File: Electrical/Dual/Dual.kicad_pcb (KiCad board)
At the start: 2 copper layers, 140 x 70 mm, 193 parts, among them J101 01x04, J102 02x04, J103 01x04, J104 01x03, J105 01x03, J106 01x03, J107 01x03, J108 01x03, J109 01x03, J110 01x04, J111 01x04, J112 01x04, J113 01x04, J114 01x03, J115 01x03, J116 01x03, J117 01x03, J201 01x03, J202 01x04, J203 01x03, J204 01x04, J205 01x03, J206 USB_OTG, J207 01x04, J208 01x02, J209 01x04, J210 01x02, J211 01x02, J212 4PostTerm, J213 2PostTerm, J214 2PostTerm, J215 2PostTerm, J216 2PostTerm, J217 2PostTerm, J218 01x02, J219 01x02, Q201 FDC6420C, Q202 FDG1024NZ, Q301 FDC6420C, Q401 FDC6420C, U201 TPD4S012, U202 ACS723LLCTR-05AB-T, U203 ACS723LLCTR-05AB-T, U204 24LC256, U205 LM2576HVS-ADJ, U206 LM2576HVS-ADJ, x100 02x05, x101 RoutaCell, x102 RoutaCell, x103 RoutaCell, x104 RoutaCell, x105 RoutaCell, x106 RoutaCell, x107 RoutaCell, x108 RoutaCell, x109 RoutaCell, x110 RoutaCell, x111 RoutaCell, x112 RoutaCell, x113 RoutaCell, x114 RoutaCell, x115 RoutaCell, x116 RoutaCell, x117 RoutaCell, x118 RoutaCell, x119 RoutaCell, x120 RoutaCell, x121 RoutaCell, x122 RoutaCell, x123 RoutaCell, x124 RoutaCell, x125 RoutaCell, x126 RoutaCell, x127 RoutaCell, x128 RoutaCell, x129 RoutaCell, x130 RoutaCell, x131 RoutaCell, x132 RoutaCell, x133 RoutaCell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

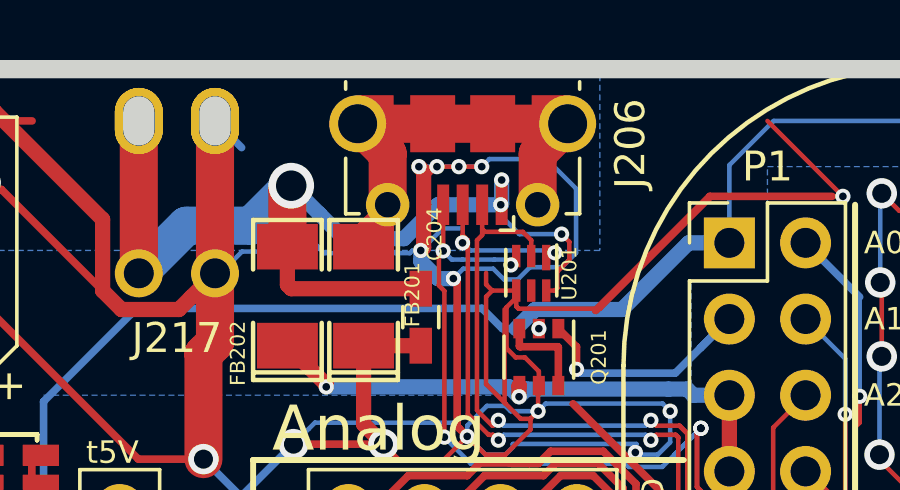
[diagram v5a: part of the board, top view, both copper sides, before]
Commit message: Fixed footprint (kicad library is wrong?)
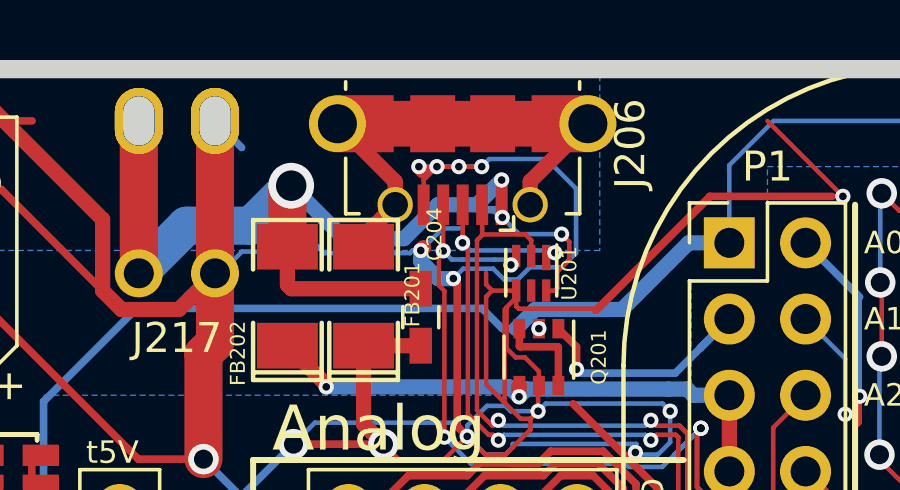
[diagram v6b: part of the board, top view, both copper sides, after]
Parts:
- removed the R205 at (61.1, 87.6) (x2)
- removed the R206 at (62.4, 114.0) (x2)
- removed the RN209 at (62.2, 79.2) (x2)
- added R205 (x2): 12K, Resistors_SMD:R_0603_HandSoldering, F.Cu at (61.1, 87.6)
- added R206 (x2): 12K, Resistors_SMD:R_0603_HandSoldering, F.Cu at (62.4, 114.0)
- added RN209 (x2): 1K2, footprints:R_Array_1206x04, F.Cu at (62.2, 79.2)
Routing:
- net GND: track 2644.4 -> 2641.8 mm
- net Net-(FB201-Pad2): track 15.0 -> 17.2 mm
- net /Common/usb1_5V: track 33.4 -> 35.4 mm

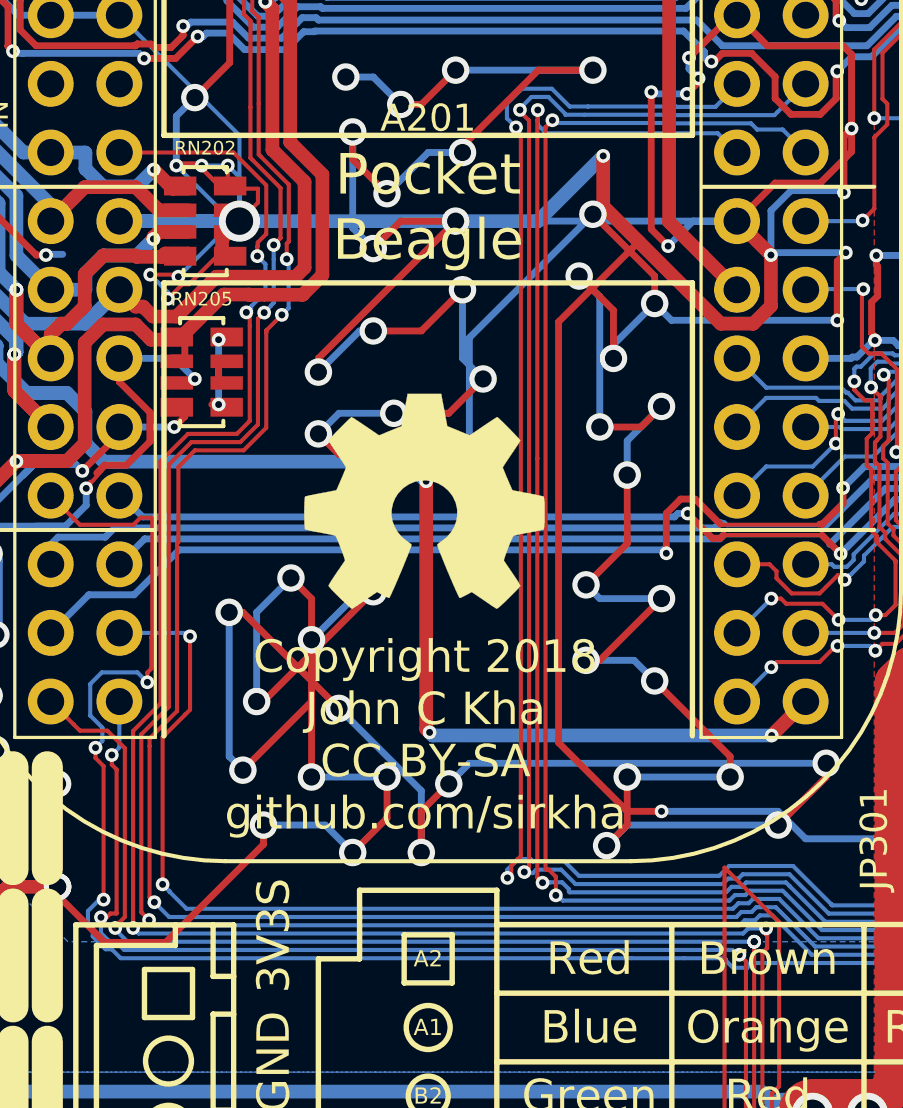
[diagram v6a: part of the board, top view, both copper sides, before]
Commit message: Modified ground viaing for better soldering.
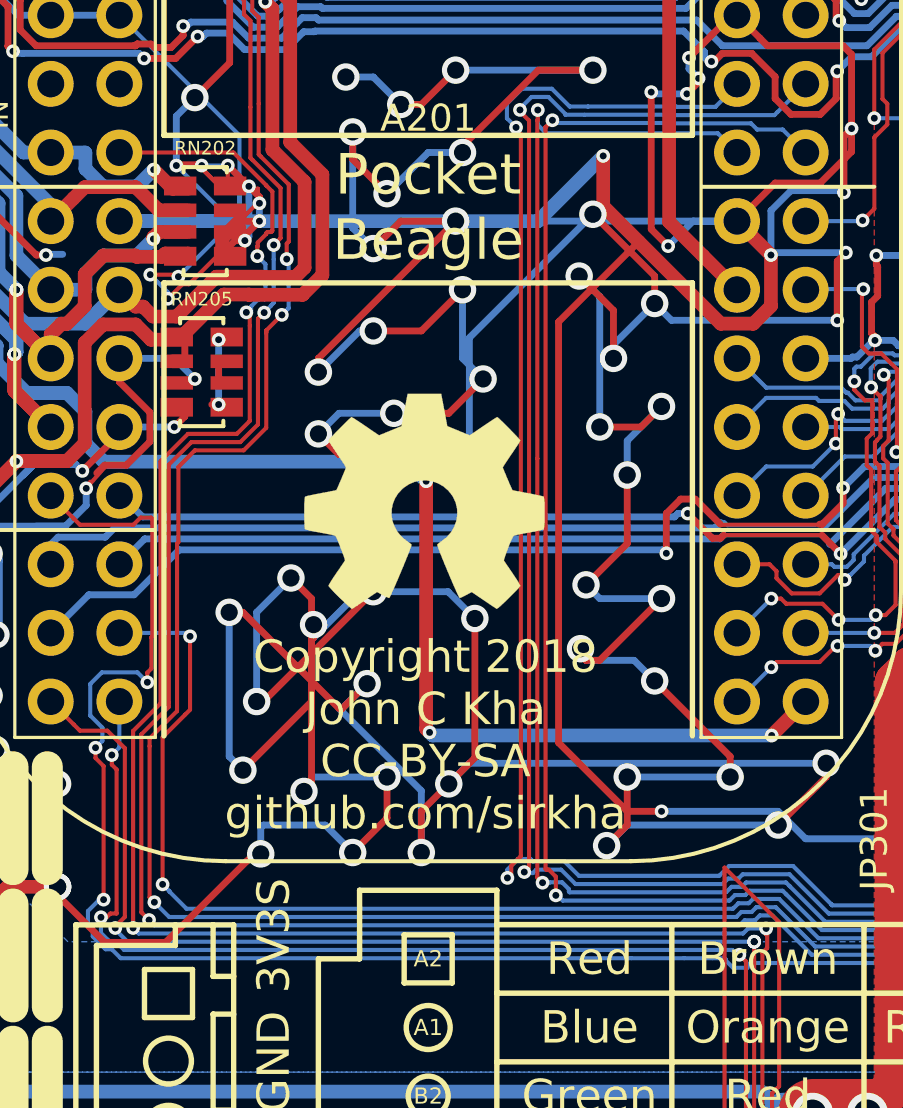
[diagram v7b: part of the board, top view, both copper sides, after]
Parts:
- removed the R205 at (61.1, 87.6) (x2)
- removed the R206 at (62.4, 114.0) (x2)
- removed the RN209 at (62.2, 79.2) (x2)
- added R205 (x2): 12K, Resistors_SMD:R_0603_HandSoldering, F.Cu at (61.1, 87.6)
- added R206 (x2): 12K, Resistors_SMD:R_0603_HandSoldering, F.Cu at (62.4, 114.0)
- added RN209 (x2): 1K2, footprints:R_Array_1206x04, F.Cu at (62.2, 79.2)
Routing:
- net GND: track 2641.8 -> 2666.1 mm, vias 386 -> 390

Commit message: Project output updated
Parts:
- removed the R205 at (61.1, 87.6) (x2)
- removed the R206 at (62.4, 114.0) (x2)
- removed the RN209 at (62.2, 79.2) (x2)
- added R205 (x2): 12K, Resistors_SMD:R_0603_HandSoldering, F.Cu at (61.1, 87.6)
- added R206 (x2): 12K, Resistors_SMD:R_0603_HandSoldering, F.Cu at (62.4, 114.0)
- added RN209 (x2): 1K2, footprints:R_Array_1206x04, F.Cu at (62.2, 79.2)
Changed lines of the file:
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@@
     (visible_elements FFFFFF7F)
     (pcbplotparams
-      (layerselection 0x00000_80000001)
+      (layerselection 0x010f0_80000001)
       (usegerberextensions false)
       (excludeedgelayer false)
@@
       (padsonsilk false)
       (subtractmaskfromsilk false)
-      (outputformat 5)
+      (outputformat 1)
       (mirror false)
       (drillshape 0)
       (scaleselection 1)
-      (outputdirectory /home/jkha/))
+      (outputdirectory Gerber/))
   )
   (net 0 "")
